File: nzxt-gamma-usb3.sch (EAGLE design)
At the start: 5 parts, among them J1 SJ1-3545N, J2 SJ1-3545N, J3 GSB311131HR, J4 GSB311131HR

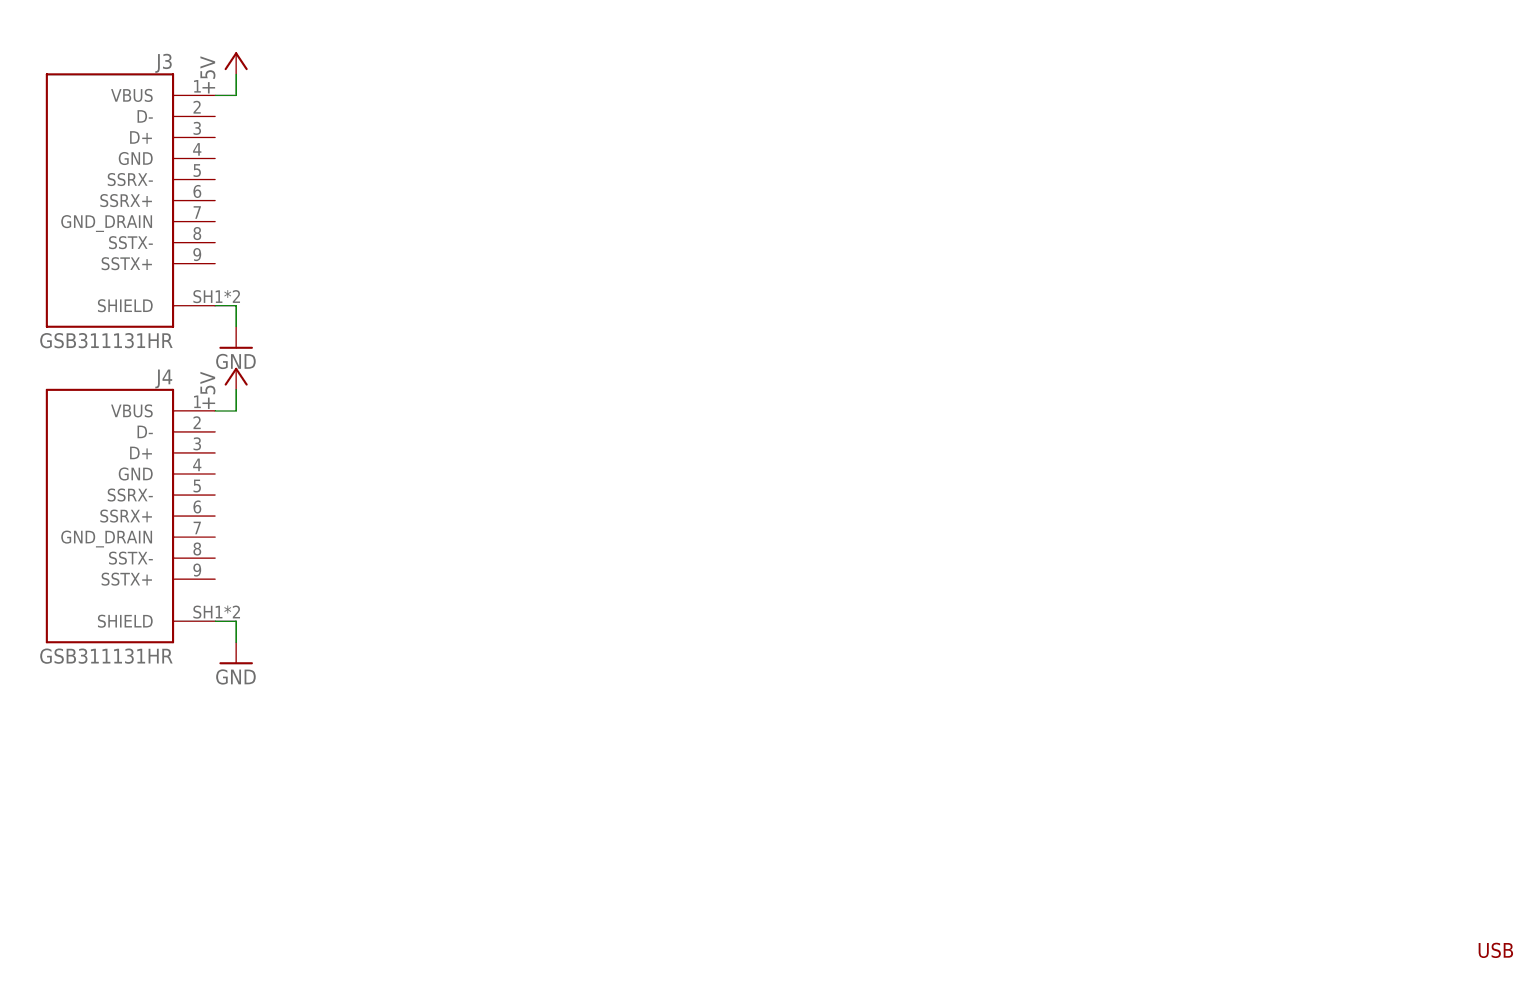
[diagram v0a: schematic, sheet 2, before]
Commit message: Added USB 3 IDC connector
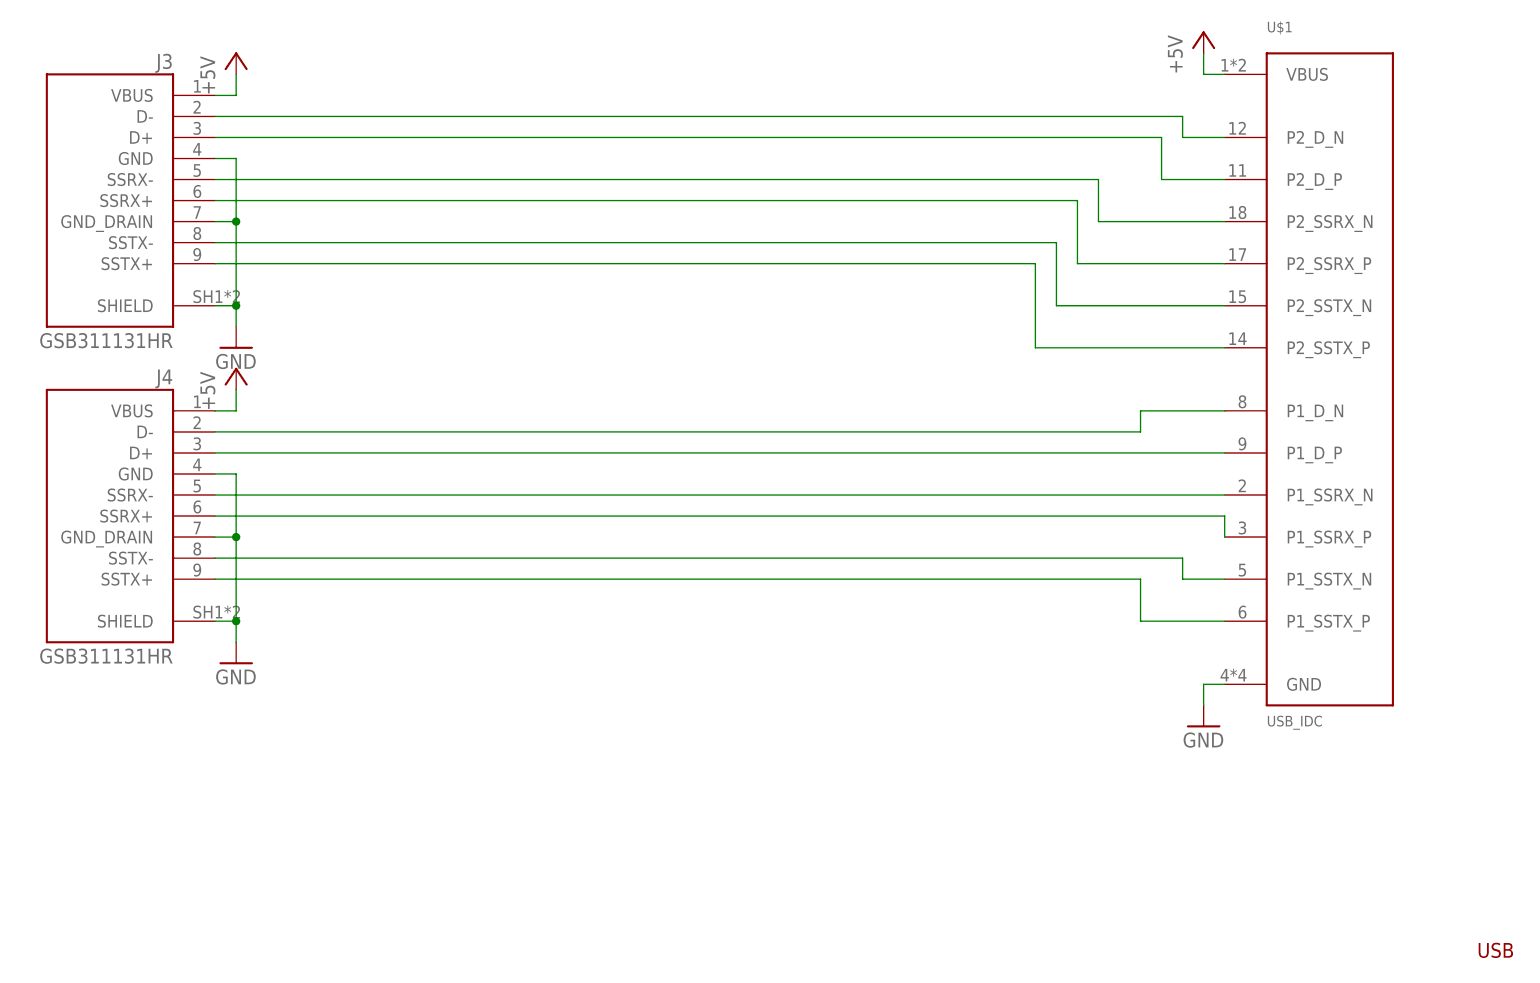
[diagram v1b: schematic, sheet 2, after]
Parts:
- added U$1: USB_IDC, usb3_idc:USB_IDC
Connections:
- new net N$10: J3.D+, U$1.P2_D_P
- new net N$11: J3.SSRX-, U$1.P2_SSRX_N
- new net N$12: J3.SSRX+, U$1.P2_SSRX_P
- new net N$13: J3.SSTX-, U$1.P2_SSTX_N
- new net N$14: J3.SSTX+, U$1.P2_SSTX_P
- new net N$15: J4.D-, U$1.P1_D_N
- new net N$16: J4.D+, U$1.P1_D_P
- new net N$17: J4.SSRX-, U$1.P1_SSRX_N
- new net N$18: J4.SSRX+, U$1.P1_SSRX_P
- new net N$19: J4.SSTX-, U$1.P1_SSTX_N
- new net N$20: J4.SSTX+, U$1.P1_SSTX_P
- new net N$9: J3.D-, U$1.P2_D_N
- net +5V: now also U$1.VBUS
- net GND: now also J3.GND, J3.GND_DRAIN, J4.GND, J4.GND_DRAIN, U$1.GND
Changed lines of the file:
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@@
 <drawing>
 <settings>
-<setting alwaysvectorfont="no"/>
+<setting alwaysvectorfont="yes"/>
 <setting verticaltext="up"/>
 </settings>
@@
 <part name="AGND2" library="supply1" library_urn="urn:adsk.eagle:library:371" deviceset="AGND" device=""/>
 <part name="AGND3" library="supply1" library_urn="urn:adsk.eagle:library:371" deviceset="AGND" device=""/>
+<part name="U$1" library="usb3_idc" deviceset="USB_IDC" device=""/>
+<part name="P+3" library="supply1" library_urn="urn:adsk.eagle:library:371" deviceset="+5V" device=""/>
+<part name="GND3" library="supply1" library_urn="urn:adsk.eagle:library:371" deviceset="GND" device=""/>
 </parts>
 <sheets>
@@
 <instance part="JP1" gate="A" x="187.96" y="104.14"/>
 <instance part="AGND1" gate="VR1" x="205.74" y="101.6"/>
-<instance part="AGND2" gate="VR1" x="104.14" y="132.08"/>
+<instance part="AGND2" gate="VR1" x="106.68" y="132.08"/>
 <instance part="AGND3" gate="VR1" x="106.68" y="91.44"/>
 </instances>
@@
 <pinref part="J1" gate="G$1" pin="1"/>
 <pinref part="AGND2" gate="VR1" pin="AGND"/>
-<wire x1="91.44" y1="134.62" x2="104.14" y2="134.62" width="0.1524" layer="91"/>
+<wire x1="91.44" y1="134.62" x2="106.68" y2="134.62" width="0.1524" layer="91"/>
 </segment>
 <segment>
@@
 <instance part="P+1" gate="1" x="68.58" y="129.54"/>
 <instance part="P+2" gate="1" x="68.58" y="91.44"/>
+<instance part="U$1" gate="G$1" x="200.66" y="91.44"/>
+<instance part="P+3" gate="1" x="185.42" y="132.08"/>
+<instance part="GND3" gate="1" x="185.42" y="48.26"/>
 </instances>
 <busses>
@@
 <wire x1="68.58" y1="86.36" x2="68.58" y2="88.9" width="0.1524" layer="91"/>
 </segment>
+<segment>
+<pinref part="P+3" gate="1" pin="+5V"/>
+<pinref part="U$1" gate="G$1" pin="VBUS"/>
+<wire x1="185.42" y1="129.54" x2="185.42" y2="127" width="0.1524" layer="91"/>
+<wire x1="185.42" y1="127" x2="187.96" y2="127" width="0.1524" layer="91"/>
+</segment>
 </net>
 <net name="GND" class="0">
@@
 <wire x1="66.04" y1="99.06" x2="68.58" y2="99.06" width="0.1524" layer="91"/>
 <wire x1="68.58" y1="99.06" x2="68.58" y2="96.52" width="0.1524" layer="91"/>
+<pinref part="J3" gate="G$1" pin="GND_DRAIN"/>
+<wire x1="66.04" y1="109.22" x2="68.58" y2="109.22" width="0.1524" layer="91"/>
+<wire x1="68.58" y1="109.22" x2="68.58" y2="99.06" width="0.1524" layer="91"/>
+<junction x="68.58" y="99.06"/>
+<pinref part="J3" gate="G$1" pin="GND"/>
+<wire x1="66.04" y1="116.84" x2="68.58" y2="116.84" width="0.1524" layer="91"/>
+<wire x1="68.58" y1="116.84" x2="68.58" y2="109.22" width="0.1524" layer="91"/>
+<junction x="68.58" y="109.22"/>
 </segment>
 <segment>
@@
 <wire x1="66.04" y1="60.96" x2="68.58" y2="60.96" width="0.1524" layer="91"/>
 <wire x1="68.58" y1="60.96" x2="68.58" y2="58.42" width="0.1524" layer="91"/>
-</segment>
-</net>
+<pinref part="J4" gate="G$1" pin="GND_DRAIN"/>
+<wire x1="66.04" y1="71.12" x2="68.58" y2="71.12" width="0.1524" layer="91"/>
+<wire x1="68.58" y1="71.12" x2="68.58" y2="60.96" width="0.1524" layer="91"/>
+<junction x="68.58" y="60.96"/>
+<pinref part="J4" gate="G$1" pin="GND"/>
+<wire x1="66.04" y1="78.74" x2="68.58" y2="78.74" width="0.1524" layer="91"/>
+<wire x1="68.58" y1="78.74" x2="68.58" y2="71.12" width="0.1524" layer="91"/>
+<junction x="68.58" y="71.12"/>
+</segment>
+<segment>
+<pinref part="U$1" gate="G$1" pin="GND"/>
+<pinref part="GND3" gate="1" pin="GND"/>
+<wire x1="187.96" y1="53.34" x2="185.42" y2="53.34" width="0.1524" layer="91"/>
+<wire x1="185.42" y1="53.34" x2="185.42" y2="50.8" width="0.1524" layer="91"/>
+</segment>
+</net>
+<net name="N$9" class="0">
+<segment>
+<pinref part="J3" gate="G$1" pin="D-"/>
+<wire x1="66.04" y1="121.92" x2="182.88" y2="121.92" width="0.1524" layer="91"/>
+<wire x1="182.88" y1="121.92" x2="182.88" y2="119.38" width="0.1524" layer="91"/>
+<pinref part="U$1" gate="G$1" pin="P2_D_N"/>
+<wire x1="182.88" y1="119.38" x2="187.96" y2="119.38" width="0.1524" layer="91"/>
+</segment>
+</net>
+<net name="N$10" class="0">
+<segment>
+<pinref part="U$1" gate="G$1" pin="P2_D_P"/>
+<wire x1="187.96" y1="114.3" x2="180.34" y2="114.3" width="0.1524" layer="91"/>
+<wire x1="180.34" y1="114.3" x2="180.34" y2="119.38" width="0.1524" layer="91"/>
+<pinref part="J3" gate="G$1" pin="D+"/>
+<wire x1="180.34" y1="119.38" x2="66.04" y2="119.38" width="0.1524" layer="91"/>
+</segment>
+</net>
+<net name="N$11" class="0">
+<segment>
+<pinref part="U$1" gate="G$1" pin="P2_SSRX_N"/>
+<wire x1="187.96" y1="109.22" x2="172.72" y2="109.22" width="0.1524" layer="91"/>
+<wire x1="172.72" y1="109.22" x2="172.72" y2="114.3" width="0.1524" layer="91"/>
+<pinref part="J3" gate="G$1" pin="SSRX-"/>
+<wire x1="172.72" y1="114.3" x2="66.04" y2="114.3" width="0.1524" layer="91"/>
+</segment>
+</net>
+<net name="N$12" class="0">
+<segment>
+<pinref part="J3" gate="G$1" pin="SSRX+"/>
+<wire x1="66.04" y1="111.76" x2="170.18" y2="111.76" width="0.1524" layer="91"/>
+<wire x1="170.18" y1="111.76" x2="170.18" y2="104.14" width="0.1524" layer="91"/>
+<pinref part="U$1" gate="G$1" pin="P2_SSRX_P"/>
+<wire x1="170.18" y1="104.14" x2="187.96" y2="104.14" width="0.1524" layer="91"/>
+</segment>
+</net>
+<net name="N$13" class="0">
+<segment>
+<pinref part="J3" gate="G$1" pin="SSTX-"/>
+<wire x1="66.04" y1="106.68" x2="167.64" y2="106.68" width="0.1524" layer="91"/>
+<pinref part="U$1" gate="G$1" pin="P2_SSTX_N"/>
+<wire x1="167.64" y1="106.68" x2="167.64" y2="99.06" width="0.1524" layer="91"/>
+<wire x1="167.64" y1="99.06" x2="187.96" y2="99.06" width="0.1524" layer="91"/>
+</segment>
+</net>
+<net name="N$14" class="0">
+<segment>
+<pinref part="J3" gate="G$1" pin="SSTX+"/>
+<wire x1="66.04" y1="104.14" x2="165.1" y2="104.14" width="0.1524" layer="91"/>
+<wire x1="165.1" y1="104.14" x2="165.1" y2="93.98" width="0.1524" layer="91"/>
+<pinref part="U$1" gate="G$1" pin="P2_SSTX_P"/>
+<wire x1="165.1" y1="93.98" x2="187.96" y2="93.98" width="0.1524" layer="91"/>
+</segment>
+</net>
+<net name="N$15" class="0">
+<segment>
+<pinref part="J4" gate="G$1" pin="D-"/>
+<wire x1="66.04" y1="83.82" x2="177.8" y2="83.82" width="0.1524" layer="91"/>
+<wire x1="177.8" y1="83.82" x2="177.8" y2="86.36" width="0.1524" layer="91"/>
+<pinref part="U$1" gate="G$1" pin="P1_D_N"/>
+<wire x1="177.8" y1="86.36" x2="187.96" y2="86.36" width="0.1524" layer="91"/>
+</segment>
+</net>
+<net name="N$16" class="0">
+<segment>
+<pinref part="U$1" gate="G$1" pin="P1_D_P"/>
+<pinref part="J4" gate="G$1" pin="D+"/>
+<wire x1="187.96" y1="81.28" x2="66.04" y2="81.28" width="0.1524" layer="91"/>
+</segment>
+</net>
+<net name="N$17" class="0">
+<segment>
+<pinref part="J4" gate="G$1" pin="SSRX-"/>
+<pinref part="U$1" gate="G$1" pin="P1_SSRX_N"/>
+<wire x1="66.04" y1="76.2" x2="187.96" y2="76.2" width="0.1524" layer="91"/>
+</segment>
+</net>
+<net name="N$18" class="0">
+<segment>
+<pinref part="U$1" gate="G$1" pin="P1_SSRX_P"/>
+<pinref part="J4" gate="G$1" pin="SSRX+"/>
+<wire x1="187.96" y1="71.12" x2="187.96" y2="73.66" width="0.1524" layer="91"/>
+<wire x1="187.96" y1="73.66" x2="66.04" y2="73.66" width="0.1524" layer="91"/>
+</segment>
+</net>
+<net name="N$19" class="0">
+<segment>
+<pinref part="J4" gate="G$1" pin="SSTX-"/>
+<wire x1="66.04" y1="68.58" x2="182.88" y2="68.58" width="0.1524" layer="91"/>
+<wire x1="182.88" y1="68.58" x2="182.88" y2="66.04" width="0.1524" layer="91"/>
+<pinref part="U$1" gate="G$1" pin="P1_SSTX_N"/>
+<wire x1="182.88" y1="66.04" x2="187.96" y2="66.04" width="0.1524" layer="91"/>
+</segment>
+</net>
+<net name="N$20" class="0">
+<segment>
+<pinref part="U$1" gate="G$1" pin="P1_SSTX_P"/>
+<wire x1="187.96" y1="60.96" x2="177.8" y2="60.96" width="0.1524" layer="91"/>
+<pinref part="J4" gate="G$1" pin="SSTX+"/>
+<wire x1="177.8" y1="60.96" x2="177.8" y2="66.04" width="0.1524" layer="91"/>
+<wire x1="177.8" y1="66.04" x2="66.04" y2="66.04" width="0.1524" layer="91"/>
+</segment>
+</net>

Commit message: Repositioned USB and eSATA ports to match casing better. started routing USB traces.
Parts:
- added U$2: G091208300LF, G091208300LF:G091208300LF
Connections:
- net N$10 renamed P2_D_P
- net N$11 renamed P2_SSRX_N
- net N$12 renamed P2_SSRX_P
- net N$13 renamed P2_SSTX_N
- net N$14 renamed P2_SSTX_P
- net N$15 renamed P1_D_N
- net N$16 renamed P1_D_P
- net N$17 renamed P1_SSRX_N
- net N$18 renamed P1_SSRX_P
- net N$19 renamed P1_SSTX_N
- net N$20 renamed P1_SSTX_P
- net N$9 renamed P2_D_N
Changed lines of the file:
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@@
 <part name="P+3" library="supply1" library_urn="urn:adsk.eagle:library:371" deviceset="+5V" device=""/>
 <part name="GND3" library="supply1" library_urn="urn:adsk.eagle:library:371" deviceset="GND" device=""/>
+<part name="U$2" library="G091208300LF" deviceset="G091208300LF" device=""/>
+<part name="FRAME3" library="frames" library_urn="urn:adsk.eagle:library:229" deviceset="A4L-LOC" device=""/>
 </parts>
 <sheets>
@@
 </segment>
 </net>
-<net name="N$9" class="0">
+<net name="P2_D_N" class="0">
 <segment>
 <pinref part="J3" gate="G$1" pin="D-"/>
@@
 <pinref part="U$1" gate="G$1" pin="P2_D_N"/>
 <wire x1="182.88" y1="119.38" x2="187.96" y2="119.38" width="0.1524" layer="91"/>
-</segment>
-</net>
-<net name="N$10" class="0">
+<label x="81.28" y="121.92" size="1.778" layer="95"/>
+</segment>
+</net>
+<net name="P2_D_P" class="0">
 <segment>
 <pinref part="U$1" gate="G$1" pin="P2_D_P"/>
@@
 <pinref part="J3" gate="G$1" pin="D+"/>
 <wire x1="180.34" y1="119.38" x2="66.04" y2="119.38" width="0.1524" layer="91"/>
-</segment>
-</net>
-<net name="N$11" class="0">
+<label x="81.28" y="119.38" size="1.778" layer="95"/>
+</segment>
+</net>
+<net name="P2_SSRX_N" class="0">
 <segment>
 <pinref part="U$1" gate="G$1" pin="P2_SSRX_N"/>
@@
 <pinref part="J3" gate="G$1" pin="SSRX-"/>
 <wire x1="172.72" y1="114.3" x2="66.04" y2="114.3" width="0.1524" layer="91"/>
-</segment>
-</net>
-<net name="N$12" class="0">
+<label x="81.28" y="114.3" size="1.778" layer="95"/>
+</segment>
+</net>
+<net name="P2_SSRX_P" class="0">
 <segment>
 <pinref part="J3" gate="G$1" pin="SSRX+"/>
@@
 <pinref part="U$1" gate="G$1" pin="P2_SSRX_P"/>
 <wire x1="170.18" y1="104.14" x2="187.96" y2="104.14" width="0.1524" layer="91"/>
-</segment>
-</net>
-<net name="N$13" class="0">
+<label x="81.28" y="111.76" size="1.778" layer="95"/>
+</segment>
+</net>
+<net name="P2_SSTX_N" class="0">
 <segment>
 <pinref part="J3" gate="G$1" pin="SSTX-"/>
@@
 <wire x1="167.64" y1="106.68" x2="167.64" y2="99.06" width="0.1524" layer="91"/>
 <wire x1="167.64" y1="99.06" x2="187.96" y2="99.06" width="0.1524" layer="91"/>
-</segment>
-</net>
-<net name="N$14" class="0">
+<label x="81.28" y="106.68" size="1.778" layer="95"/>
+</segment>
+</net>
+<net name="P2_SSTX_P" class="0">
 <segment>
 <pinref part="J3" gate="G$1" pin="SSTX+"/>
@@
 <pinref part="U$1" gate="G$1" pin="P2_SSTX_P"/>
 <wire x1="165.1" y1="93.98" x2="187.96" y2="93.98" width="0.1524" layer="91"/>
-</segment>
-</net>
-<net name="N$15" class="0">
+<label x="81.28" y="104.14" size="1.778" layer="95"/>
+</segment>
+</net>
+<net name="P1_D_N" class="0">
 <segment>
 <pinref part="J4" gate="G$1" pin="D-"/>
@@
 <pinref part="U$1" gate="G$1" pin="P1_D_N"/>
 <wire x1="177.8" y1="86.36" x2="187.96" y2="86.36" width="0.1524" layer="91"/>
-</segment>
-</net>
-<net name="N$16" class="0">
+<label x="81.28" y="83.82" size="1.778" layer="95"/>
+</segment>
+</net>
+<net name="P1_D_P" class="0">
 <segment>
 <pinref part="U$1" gate="G$1" pin="P1_D_P"/>
 <pinref part="J4" gate="G$1" pin="D+"/>
 <wire x1="187.96" y1="81.28" x2="66.04" y2="81.28" width="0.1524" layer="91"/>
-</segment>
-</net>
-<net name="N$17" class="0">
+<label x="81.28" y="81.28" size="1.778" layer="95"/>
+</segment>
+</net>
+<net name="P1_SSRX_N" class="0">
 <segment>
 <pinref part="J4" gate="G$1" pin="SSRX-"/>
 <pinref part="U$1" gate="G$1" pin="P1_SSRX_N"/>
 <wire x1="66.04" y1="76.2" x2="187.96" y2="76.2" width="0.1524" layer="91"/>
-</segment>
-</net>
-<net name="N$18" class="0">
+<label x="81.28" y="76.2" size="1.778" layer="95"/>
+</segment>
+</net>
+<net name="P1_SSRX_P" class="0">
 <segment>
 <pinref part="U$1" gate="G$1" pin="P1_SSRX_P"/>
@@
 <wire x1="187.96" y1="71.12" x2="187.96" y2="73.66" width="0.1524" layer="91"/>
 <wire x1="187.96" y1="73.66" x2="66.04" y2="73.66" width="0.1524" layer="91"/>
-</segment>
-</net>
-<net name="N$19" class="0">
+<label x="81.28" y="73.66" size="1.778" layer="95"/>
+</segment>
+</net>
+<net name="P1_SSTX_N" class="0">
 <segment>
 <pinref part="J4" gate="G$1" pin="SSTX-"/>
@@
 <pinref part="U$1" gate="G$1" pin="P1_SSTX_N"/>
 <wire x1="182.88" y1="66.04" x2="187.96" y2="66.04" width="0.1524" layer="91"/>
-</segment>
-</net>
-<net name="N$20" class="0">
+<label x="81.28" y="68.58" size="1.778" layer="95"/>
+</segment>
+</net>
+<net name="P1_SSTX_P" class="0">
 <segment>
 <pinref part="U$1" gate="G$1" pin="P1_SSTX_P"/>
@@
 <wire x1="177.8" y1="60.96" x2="177.8" y2="66.04" width="0.1524" layer="91"/>
 <wire x1="177.8" y1="66.04" x2="66.04" y2="66.04" width="0.1524" layer="91"/>
+<label x="81.28" y="66.04" size="1.778" layer="95"/>
 </segment>
 </net>
 </nets>
 </sheet>
+<sheet>
+<plain>
+</plain>
+<instances>
+<instance part="U$2" gate="G$1" x="53.34" y="68.58" rot="MR0"/>
+<instance part="FRAME3" gate="G$1" x="0" y="0"/>
+</instances>
+<busses>
+</busses>
+<nets>
+</nets>
+</sheet>
